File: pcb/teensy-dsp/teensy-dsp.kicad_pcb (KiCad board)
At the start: 2 copper layers, 4 parts, among them J1 ACJS-IH, J2 ACJS-IH, J5 ACJS-IH, J6 ACJS-IH

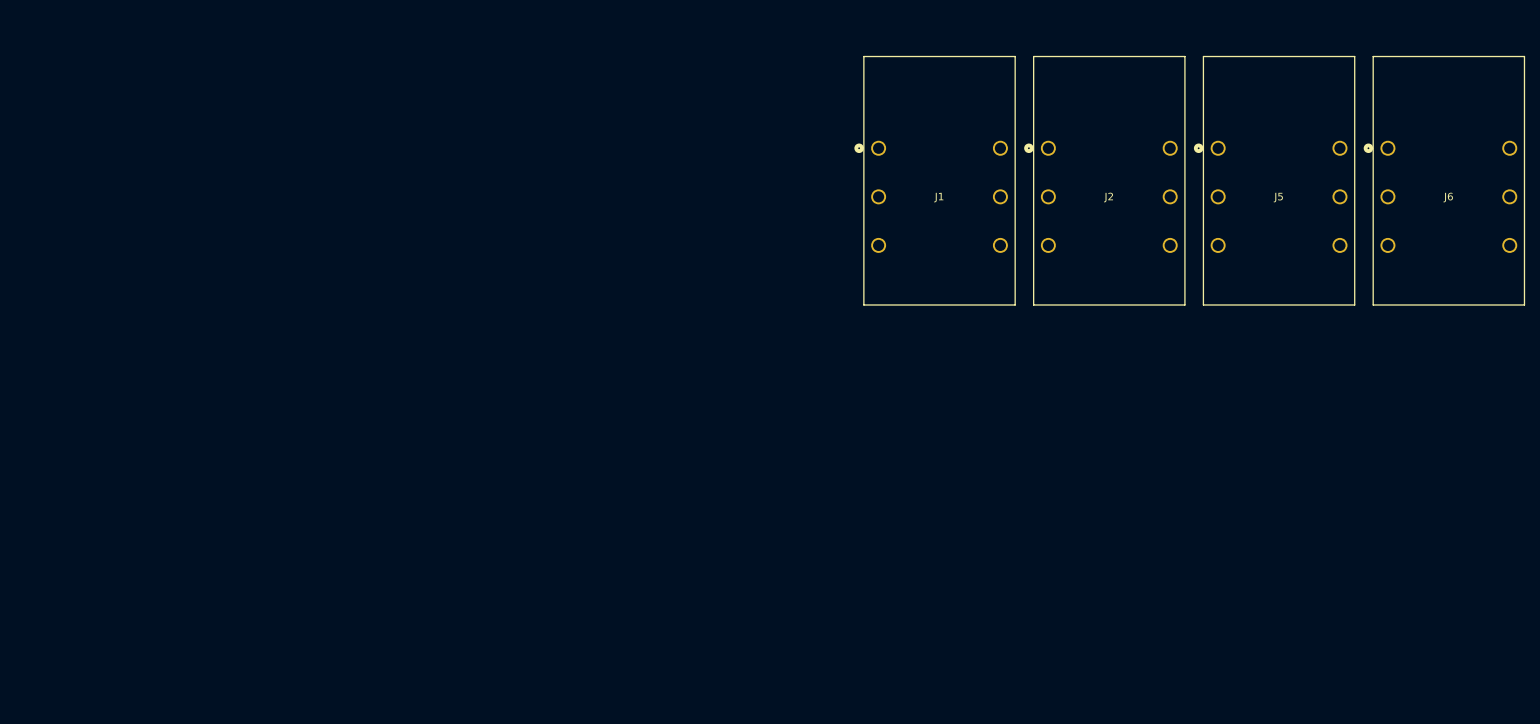
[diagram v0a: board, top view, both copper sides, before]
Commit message: update kicad and solidworks
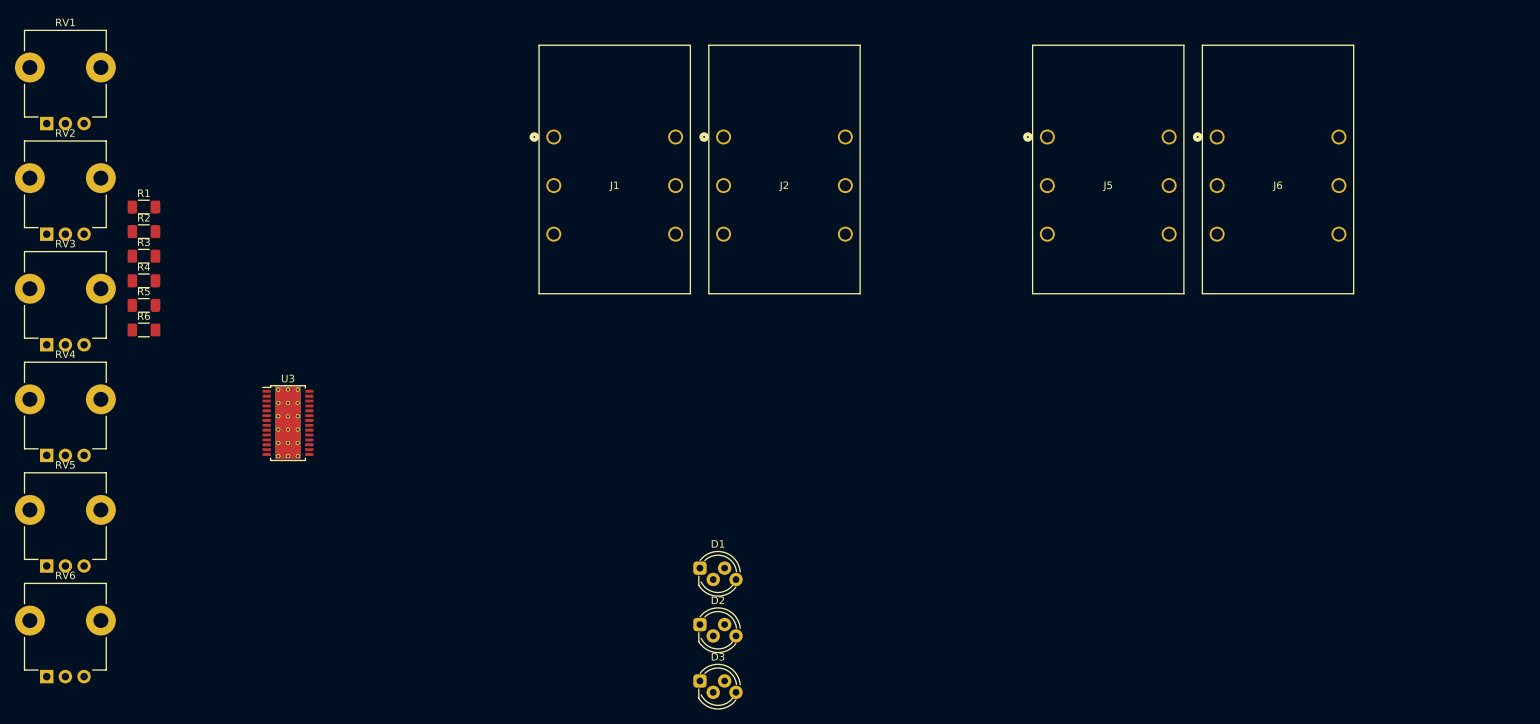
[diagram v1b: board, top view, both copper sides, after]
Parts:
- added D1: LED_RABG, LED_THT:LED_D5.0mm-4_RGB_Staggered_Pins, F.Cu at (121.2, 94.0)
- added D2: LED_RABG, LED_THT:LED_D5.0mm-4_RGB_Staggered_Pins, F.Cu at (121.2, 101.5)
- added D3: LED_RABG, LED_THT:LED_D5.0mm-4_RGB_Staggered_Pins, F.Cu at (121.2, 109.1)
- added R1: 1k91, Resistor_SMD:R_1206_3216Metric_Pad1.30x1.75mm_HandSolder, F.Cu at (46.8, 45.7)
- added R2: 100R, Resistor_SMD:R_1206_3216Metric_Pad1.30x1.75mm_HandSolder, F.Cu at (46.8, 49.0)
- added R3: 100R, Resistor_SMD:R_1206_3216Metric_Pad1.30x1.75mm_HandSolder, F.Cu at (46.8, 52.2)
- added R4: 100R, Resistor_SMD:R_1206_3216Metric_Pad1.30x1.75mm_HandSolder, F.Cu at (46.8, 55.5)
- added R5: 100R, Resistor_SMD:R_1206_3216Metric_Pad1.30x1.75mm_HandSolder, F.Cu at (46.8, 58.8)
- added R6: 100R, Resistor_SMD:R_1206_3216Metric_Pad1.30x1.75mm_HandSolder, F.Cu at (46.8, 62.1)
- added RV1: 10k, Potentiometer_THT:Potentiometer_TT_P0915N, F.Cu at (33.8, 34.5)
- added RV2: 10k, Potentiometer_THT:Potentiometer_TT_P0915N, F.Cu at (33.8, 49.3)
- added RV3: 10k, Potentiometer_THT:Potentiometer_TT_P0915N, F.Cu at (33.8, 64.1)
- added RV4: 10k, Potentiometer_THT:Potentiometer_TT_P0915N, F.Cu at (33.8, 78.9)
- added RV5: 10k, Potentiometer_THT:Potentiometer_TT_P0915N, F.Cu at (33.8, 93.7)
- added RV6: 10k, Potentiometer_THT:Potentiometer_TT_P0915N, F.Cu at (33.8, 108.5)
- added U3: TLC5940PWP, Package_SO:HTSSOP-28-1EP_4.4x9.7mm_P0.65mm_EP3.4x9.5mm_Mask2.4x6.17mm_ThermalVias, F.Cu at (66.0, 74.5)
- moved J1 43.5 mm to (101.6, 36.3)
- moved J2 43.5 mm to (124.3, 36.3)
- moved J6 22.9 mm to (190.4, 36.3)
- moved J5 22.9 mm to (167.6, 36.3)

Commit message: update pcb layout
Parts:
- removed D1, D2, D3: LED_RABG, LED_THT:LED_D5.0mm-4_RGB_Staggered_Pins
- removed R1: 1k91, Resistor_SMD:R_1206_3216Metric_Pad1.30x1.75mm_HandSolder
- removed R2, R3, R4, R5, R6: 100R, Resistor_SMD:R_1206_3216Metric_Pad1.30x1.75mm_HandSolder
- removed RV1, RV2, RV3, RV4, RV5, RV6: 10k, Potentiometer_THT:Potentiometer_TT_P0915N
- added C1: 100u 16V, Capacitor_SMD:CP_Elec_6.3x5.9, F.Cu at (147.0, 68.0)
- added C2: 100u 16V, Capacitor_SMD:CP_Elec_6.3x5.9, F.Cu at (157.0, 83.0)
- added J3: FSW1, Connector_Molex:Molex_Micro-Fit_3.0_43650-0200_1x02_P3.00mm_Horizontal, F.Cu at (131.5, 123.0)
- added J4: FSW2, Connector_Molex:Molex_Micro-Fit_3.0_43650-0200_1x02_P3.00mm_Horizontal, F.Cu at (111.5, 123.0)
- added J7: Conn_02x15_Odd_Even, Connector_IDC:IDC-Header_2x15_P2.54mm_Vertical, F.Cu at (183.0, 124.0)
- added J8: Barrel_Jack_Switch, Connector_BarrelJack:BarrelJack_CUI_PJ-102AH_Horizontal, F.Cu at (146.6, 61.0)
- added J9: USB_B_Mini, Connector_USB:USB_Mini-B_Wuerth_65100516121_Horizontal, F.Cu at (192.0, 87.0)
- added U1: Teensy4.1, Imported Footprints:MODULE_DEV-16771, F.Cu at (165.3, 105.4)
- added U2: Teensy4.0_AudioShield_REVD, Imported Footprints:4.0audioshield, F.Cu at (98.6, 105.8)
- U3: value TLC5940PWP -> LM7805_TO220; footprint Package_SO:HTSSOP-28-1EP_4.4x9.7mm_P0.65mm_EP3.4x9.5mm_Mask2.4x6.17mm_ThermalVias -> Package_TO_SOT_SMD:SOT-223
- moved U3 80.9 mm to (146.8, 78.0)
- moved J6 25.1 mm to (176.2, 57.0)
- moved J5 24.1 mm to (155.2, 57.0)
- moved J2 20.9 mm to (121.2, 57.0)
- moved J1 20.8 mm to (100.2, 57.0)
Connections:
- J1 pad R: /Audio IO/Line In LGND -> GND
- J1 pad T: /Audio IO/Line In L -> R Line Out
- J2 pad R: /Audio IO/Line In RGND -> GND
- J2 pad T: /Audio IO/Line In R -> L Line Out
- J5 pad R: /Audio IO/Line Out GND -> GND
- J5 pad T: /Audio IO/Line Out L -> R Line In
- J6 pad R: /Audio IO/Line Out GND -> GND
- J6 pad T: /Audio IO/Line Out R -> L Line In
- U3 pad 1: GND -> +9V
- U3 pad 2: Net-(U3-BLANK) -> GND
- U3 pad 3: Net-(U3-XLAT) -> +5V
- U3 pad 4: Net-(U3-SCLK) -> (no net)
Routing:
- net L Line In: track 0.00 -> 75.0 mm
- net Net-(J9-D+): track 0.00 -> 56.8 mm
- net Net-(J9-D-): track 0.00 -> 54.1 mm
- net R Line In: track 0.00 -> 50.5 mm
- net POT_5: track 0.00 -> 43.2 mm
- net POT_6: track 0.00 -> 43.2 mm
- net POT_1: track 0.00 -> 26.4 mm
- net POT_4: track 0.00 -> 26.3 mm
- net POT_3: track 0.00 -> 26.3 mm
- net POT_2: track 0.00 -> 26.3 mm
- net R Line Out: track 0.00 -> 22.9 mm
- net L Line Out: track 0.00 -> 18.2 mm
- added copper zone on In2.Cu, net +3.3V
- added copper zone on In2.Cu, net +9V
- added copper zone on In1.Cu, net GND
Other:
- board outline added: 101 x 82 mm
- copper layers 2 -> 4
- board text added: "LEFT IN"
- board text added: "LEFT OUT"
- board text added: "RIGHT IN"
- board text added: "RIGHT OUT"

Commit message: update pcb layout
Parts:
- added C3: 100n 16V, Capacitor_SMD:C_1210_3225Metric_Pad1.33x2.70mm_HandSolder, F.Cu at (152.2, 100.5)
- added D1: D, Diode_THT:D_DO-41_SOD81_P10.16mm_Horizontal, F.Cu at (146.4, 79.0)
- added R1: 47R, Resistor_SMD:R_1210_3225Metric_Pad1.30x2.65mm_HandSolder, F.Cu at (151.2, 85.0)
- moved U3 26.5 mm to (162.2, 99.7)
- moved C1 25.0 mm to (151.2, 92.7), turned to 180 degrees
- moved C2 21.7 mm to (144.2, 100.5), turned to 90 degrees
- moved J8 12.9 mm to (151.4, 73.0)
- moved J1 12.7 mm to (105.4, 68.7)
- moved J2 12.7 mm to (126.4, 68.7)
- moved J5 12.7 mm to (160.4, 68.7)
- moved J6 12.7 mm to (181.4, 68.7)
- moved U2 11.6 mm to (103.8, 116.2)
- moved J9 11.6 mm to (197.2, 97.4)
- moved U1 11.6 mm to (170.5, 115.8)
- moved J4 11.6 mm to (116.7, 133.4)
- moved J7 11.6 mm to (188.2, 134.4)
- moved J3 11.4 mm to (136.2, 133.4)
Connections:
- J1 pad T: R Line Out -> L Line In
- J2 pad T: L Line Out -> R Line In
- J5 pad T: R Line In -> L Line Out
- J6 pad T: L Line In -> R Line Out
- J8 pad 2: +9V -> Net-(D1-A)
- J9 pad 6: unconnected-(J9-Shield-Pad6) -> Earth
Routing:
- net +5V: track 0.00 -> 127.2 mm, vias 0 -> 3
- net +9V: track 0.00 -> 117.9 mm, vias 0 -> 4
- net FSW_2: track 0.00 -> 92.1 mm
- net FSW_1: track 0.00 -> 69.7 mm
- net L Line In: track 75.0 -> 19.6 mm
- net R Line Out: track 22.9 -> 71.4 mm
- net Audio MCLK: track 0.00 -> 43.5 mm
- net Audio BCLK: track 0.00 -> 43.5 mm
- net Audio LRCLK: track 0.00 -> 41.7 mm
- net Audio SCK: track 0.00 -> 41.0 mm, vias 0 -> 1
- net Audio MOSI: track 0.00 -> 40.9 mm
- net Audio SDCS: track 0.00 -> 40.6 mm
- net Audio MEMCS: track 0.00 -> 40.5 mm
- net Audio SCL: track 0.00 -> 40.5 mm
- net Audio DOUT: track 0.00 -> 40.5 mm
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- added copper zone on F.Cu, net Earth
- added copper zone on B.Cu, net GND
- added copper zone on F.Cu, net GND
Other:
- board size 101 x 82 mm -> 101 x 76.8 mm

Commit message: pcb and case updates
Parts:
- removed J3: FSW1, Connector_Molex:Molex_Micro-Fit_3.0_43650-0200_1x02_P3.00mm_Horizontal
- removed J4: FSW2, Connector_Molex:Molex_Micro-Fit_3.0_43650-0200_1x02_P3.00mm_Horizontal
- J9: moved to B.Cu
- moved J8 65.3 mm to (215.0, 58.0)
- moved C2 57.5 mm to (145.0, 43.0)
- moved C3 57.0 mm to (155.0, 43.6)
- moved U3 49.9 mm to (151.0, 51.0)
- moved C1 49.9 mm to (166.0, 45.0)
- moved D1 44.2 mm to (175.9, 46.0)
- moved R1 40.5 mm to (176.0, 53.0)
- moved J9 30.7 mm to (221.0, 78.0), turned to -90 degrees
- moved U1 15.2 mm to (165.8, 101.3)
- moved J7 14.8 mm to (183.5, 120.3)
- moved J5 8.69 mm to (151.7, 69.0)
- moved J6 8.69 mm to (172.7, 69.0)
- moved J1 4.70 mm to (100.7, 69.0)
- moved J2 4.70 mm to (121.7, 69.0)
- moved U2 4.70 mm to (99.1, 116.6)
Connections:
- J7 pad 11: LED_BLANK -> LED_SCLK
- J7 pad 15: LED_SCLK -> LED_BLANK
- J7 pad 3: +9V -> +3.3V
- J7 pad 5: +5V -> FSW_2
- J7 pad 7: +3.3V -> FSW_1
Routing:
- net +5V: track 127.2 -> 0.00 mm, vias 3 -> 0
- net +9V: track 117.9 -> 0.00 mm, vias 4 -> 0
- net FSW_2: track 92.1 -> 0.00 mm
- net R Line Out: track 71.4 -> 0.00 mm
- net FSW_1: track 69.7 -> 0.00 mm
- net Net-(J9-D-): track 55.0 -> 0.00 mm
- net Net-(J9-D+): track 51.7 -> 0.00 mm
- net POT_6: track 45.7 -> 0.00 mm
- net POT_5: track 45.2 -> 0.00 mm
- net Audio MCLK: track 43.5 -> 0.00 mm
- net Audio BCLK: track 43.5 -> 0.00 mm
- net Audio LRCLK: track 41.7 -> 0.00 mm
- net L Line Out: track 41.5 -> 0.00 mm
- net Audio SCK: track 41.0 -> 0.00 mm, vias 1 -> 0
- net Audio MOSI: track 40.9 -> 0.00 mm
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- removed copper zone on In2.Cu, net +3.3V
- removed copper zone on In2.Cu, net +9V
- removed copper zone on F.Cu, net Earth
- removed copper zone on B.Cu, net GND
- removed copper zone on F.Cu, net GND
- removed copper zone on In1.Cu, net GND
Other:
- board size 101 x 76.8 mm -> 106 x 66.7 mm

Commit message: case updates
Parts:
- D1: footprint Diode_THT:D_DO-41_SOD81_P10.16mm_Horizontal -> Diode_SMD:D_SOD-123
- U3: footprint Package_TO_SOT_SMD:SOT-223 -> Package_TO_SOT_SMD:TO-252-3_TabPin2
- moved U3 111.7 mm to (262.5, 58.7)
- moved D1 88.1 mm to (260.9, 23.0)
- moved C1 88.1 mm to (251.0, 22.0)
- moved C2 88.1 mm to (230.0, 20.0)
- moved C3 88.1 mm to (240.0, 20.6)
- moved R1 88.1 mm to (261.0, 30.0)
- moved U1 80.4 mm to (246.0, 107.6)
- moved J1 47.5 mm to (132.4, 33.7)
- moved J2 47.5 mm to (153.4, 33.7)
- moved J5 47.5 mm to (183.4, 33.7)
- moved J6 47.5 mm to (204.4, 33.7)
- moved J7 44.3 mm to (227.6, 123.6)
- moved U2 44.3 mm to (143.2, 119.8)
- moved J8 23.1 mm to (238.0, 56.0)
- moved J9 23.1 mm to (244.0, 76.0)
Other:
- board size 106 x 66.7 mm -> 105 x 65 mm
